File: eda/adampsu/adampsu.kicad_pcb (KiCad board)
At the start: 2 copper layers, 12 parts, among them J1 Barrel_Jack_Switch, U1 LM27761, U2 LT1084-5.0

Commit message: BOM completeled but using expensive LDO
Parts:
- removed C1, C5, C6: 4.7uF, Capacitor_SMD:C_1206_3216Metric_Pad1.42x1.75mm_HandSolder
- removed C2: 1uF, Capacitor_SMD:C_0603_1608Metric_Pad1.05x0.95mm_HandSolder
- removed C3: 10uF, Capacitor_SMD:C_1206_3216Metric_Pad1.42x1.75mm_HandSolder
- removed C4: 22uF, Capacitor_SMD:C_1206_3216Metric_Pad1.42x1.75mm_HandSolder
- removed D1: B240, Diode_SMD:D_SMB
- removed J1: Barrel_Jack_Switch, Connector_BarrelJack:BarrelJack_Horizontal
- removed R1: 1.55M, Capacitor_SMD:C_0603_1608Metric_Pad1.05x0.95mm_HandSolder
- removed R2: 500k, Capacitor_SMD:C_0603_1608Metric_Pad1.05x0.95mm_HandSolder
- removed U1: LM27761, Package_SON:WSON-8-1EP_2x2mm_P0.5mm_EP0.9x1.6mm
- removed U2: LT1084-5.0, Package_TO_SOT_THT:TO-220-3_Vertical

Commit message: Final parts selection finished
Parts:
- added C1: 4.7uF, Capacitor_SMD:C_1206_3216Metric_Pad1.42x1.75mm_HandSolder, F.Cu at (139.4, 106.6)
- added C10: 0.01uF, Capacitor_SMD:C_0603_1608Metric_Pad1.05x0.95mm_HandSolder, F.Cu at (143.3, 109.5)
- added C11: 2200pF, Capacitor_SMD:C_0603_1608Metric_Pad1.05x0.95mm_HandSolder, F.Cu at (144.5, 106.2)
- added C12: 22pF, Capacitor_SMD:C_0603_1608Metric_Pad1.05x0.95mm_HandSolder, F.Cu at (134.7, 113.7)
- added C13: 47uF, Capacitor_SMD:C_1210_3225Metric_Pad1.42x2.65mm_HandSolder, F.Cu at (133.4, 110.3)
- added C14: 47uF, Capacitor_SMD:C_1210_3225Metric_Pad1.42x2.65mm_HandSolder, F.Cu at (157.9, 90.5)
- added C15: 0.01uF, Capacitor_SMD:C_0603_1608Metric_Pad1.05x0.95mm_HandSolder, F.Cu at (153.6, 96.4)
- added C16: 0.1uF, Capacitor_SMD:C_0603_1608Metric_Pad1.05x0.95mm_HandSolder, F.Cu at (163.0, 89.7)
- added C2: 1uF, Capacitor_SMD:C_0603_1608Metric_Pad1.05x0.95mm_HandSolder, F.Cu at (157.9, 93.9)
- added C3: 100uF, Capacitor_THT:CP_Radial_D8.0mm_P3.50mm, F.Cu at (158.1, 83.7)
- added C4: 4.7uF, Capacitor_SMD:C_1206_3216Metric_Pad1.42x1.75mm_HandSolder, F.Cu at (108.8, 112.5)
- added C5: 10uF, Capacitor_SMD:C_0805_2012Metric_Pad1.15x1.40mm_HandSolder, F.Cu at (130.2, 113.9)
- added C6: 4.7uF, Capacitor_SMD:C_1206_3216Metric_Pad1.42x1.75mm_HandSolder, F.Cu at (102.8, 112.5)
- added C7: 4.7uF, Capacitor_SMD:C_1206_3216Metric_Pad1.42x1.75mm_HandSolder, F.Cu at (133.4, 106.6)
- added C8: 0.01uF, Capacitor_SMD:C_0603_1608Metric_Pad1.05x0.95mm_HandSolder, F.Cu at (153.6, 93.9)
- added C9: 0.1uF, adampsu:C_0508_1220Metric_Pad1.40x1.15mm_HandSolder, F.Cu at (138.8, 110.0)
- added D1: D_Schottky, Diode_SMD:D_SMC_Handsoldering, F.Cu at (107.3, 106.9)
- added D2: D_Schottky, Diode_SMD:D_SMC_Handsoldering, F.Cu at (107.3, 97.8)
- added J1: Barrel_Jack_Switch, adampsu:BarrelJack_CUI_PJ-047AH_Horizontal, F.Cu at (145.8, 95.3)
- added J2: Conn_2Rows-09Pins, Connector_PinHeader_2.54mm:PinHeader_2x05_P2.54mm_Vertical, F.Cu at (117.0, 96.3)
- added J3: DB9_Female, Connector_Dsub:DSUB-9_Female_Vertical_P2.77x2.84mm_MountingHoles, F.Cu at (121.9, 85.2)
- added L1: 4.7uH, adampsu:L_11.5x10.3_H4.8, F.Cu at (147.6, 84.9)
- added PC1: PlungerCap, adampsu:PlungerCap-4JWHT, F.Cu at (121.2, 109.5)
- added Q1: BUK7880-55A_CUX, Package_TO_SOT_SMD:SOT-223-3_TabPin2, F.Cu at (126.8, 98.1)
- added R1: 1.55M, Resistor_SMD:R_0603_1608Metric_Pad1.05x0.95mm_HandSolder, F.Cu at (153.6, 103.9)
- added R10: 1.96k, Resistor_SMD:R_0603_1608Metric_Pad1.05x0.95mm_HandSolder, F.Cu at (139.1, 113.1)
- added R2: 500k, Resistor_SMD:R_0603_1608Metric_Pad1.05x0.95mm_HandSolder, F.Cu at (147.7, 108.7)
- added R3: 1k, Resistor_SMD:R_0603_1608Metric_Pad1.05x0.95mm_HandSolder, F.Cu at (143.4, 112.0)
- added R4: 10k, Resistor_SMD:R_0603_1608Metric_Pad1.05x0.95mm_HandSolder, F.Cu at (157.9, 98.9)
- added R5: 665k, Resistor_SMD:R_0603_1608Metric_Pad1.05x0.95mm_HandSolder, F.Cu at (153.6, 98.9)
- added R6: 130k, Resistor_SMD:R_0603_1608Metric_Pad1.05x0.95mm_HandSolder, F.Cu at (163.0, 92.2)
- added R7: 37.4k, Resistor_SMD:R_0603_1608Metric_Pad1.05x0.95mm_HandSolder, F.Cu at (153.6, 101.4)
- added R8: 51.1, Resistor_SMD:R_0603_1608Metric_Pad1.05x0.95mm_HandSolder, F.Cu at (157.9, 96.4)
- added R9: 10.2k, Resistor_SMD:R_0603_1608Metric_Pad1.05x0.95mm_HandSolder, F.Cu at (148.9, 106.2)
- added SW1: 30V 300mA Latching Switch, adampsu:Switch-LC1258EENP, F.Cu at (136.3, 86.1)
- added U1: LM27761, Package_SON:WSON-8-1EP_2x2mm_P0.5mm_EP0.9x1.6mm, F.Cu at (157.9, 101.9)
- added U2: TPS54531DDAR, Package_SO:TI_SO-PowerPAD-8_ThermalVias, F.Cu at (126.2, 105.5)

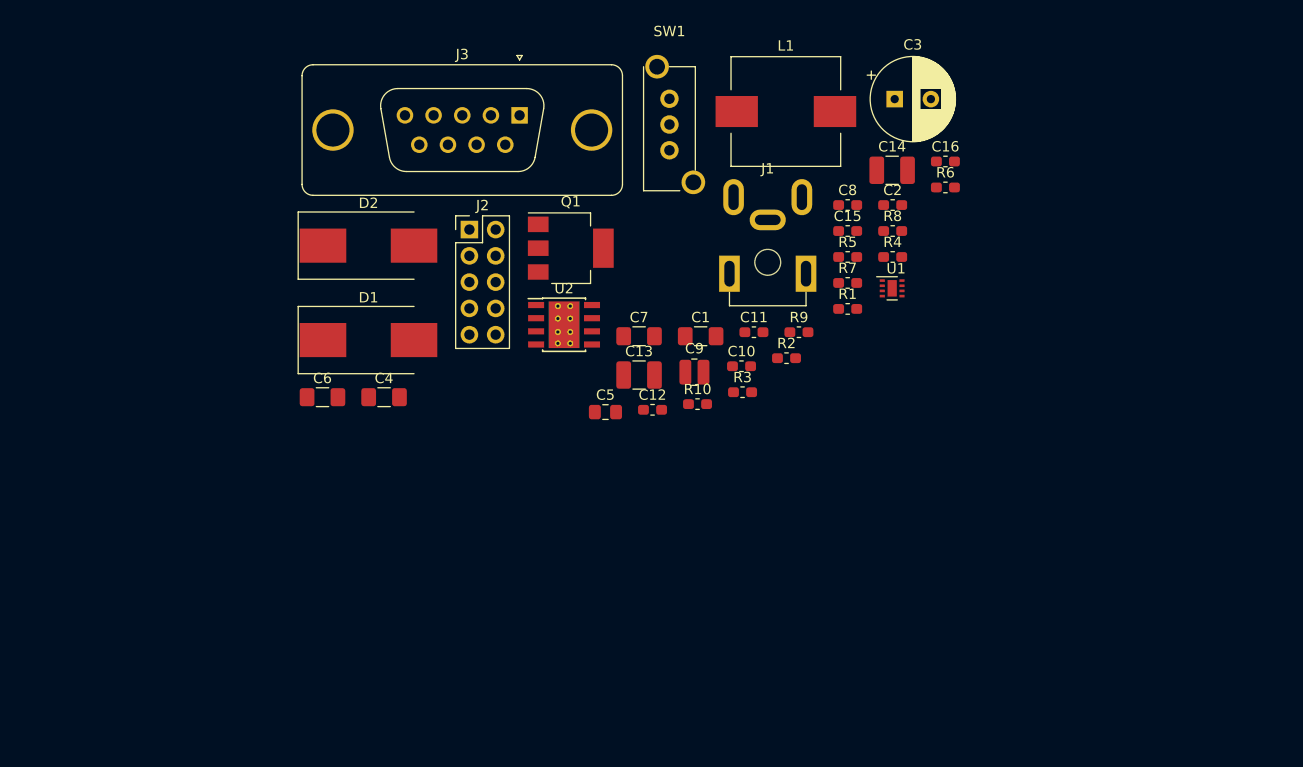
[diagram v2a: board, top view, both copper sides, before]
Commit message: board layout started, but need new -5V regulator
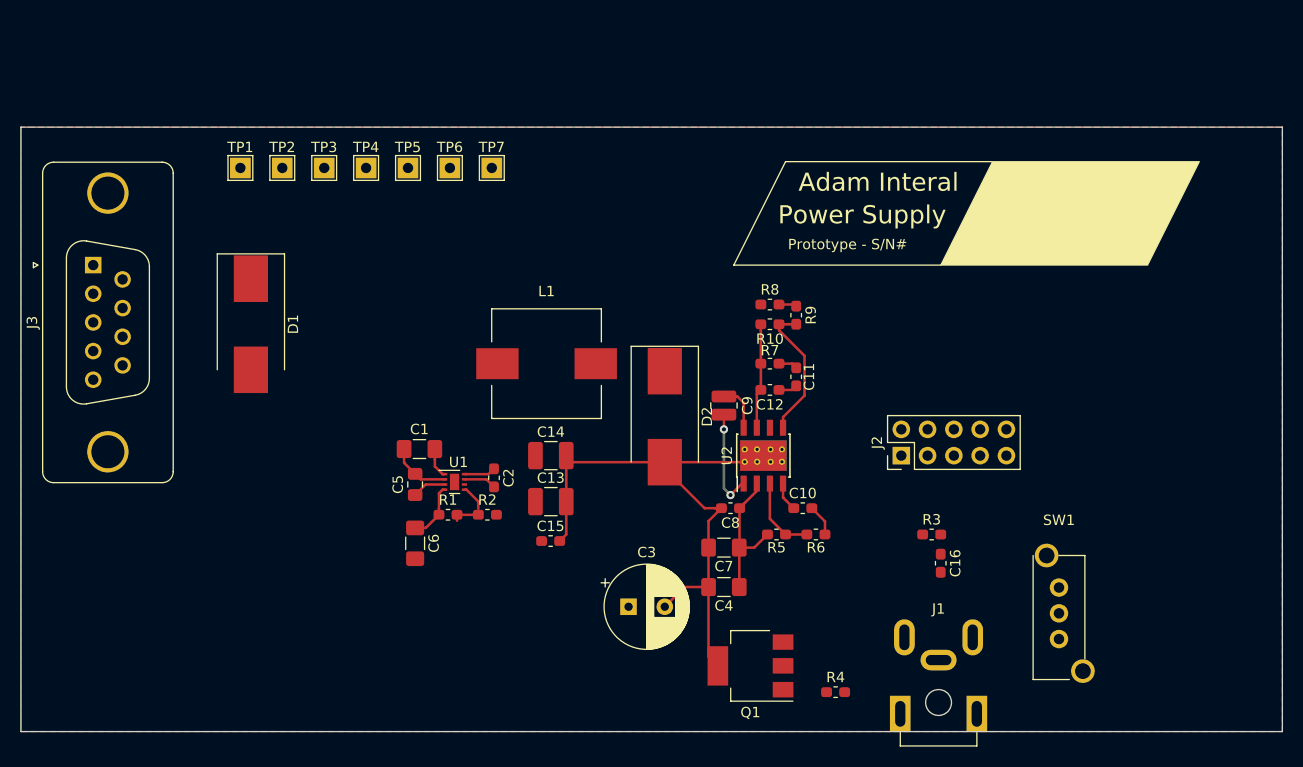
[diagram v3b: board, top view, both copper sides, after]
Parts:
- added LB1: HandLabel_SN, adampsu:adamlabel, F.Cu at (162.6, 99.7)
- added TP1: TestPoint, TestPoint:TestPoint_THTPad_2.0x2.0mm_Drill1.0mm, F.Cu at (94.9, 90.3)
- added TP2: TestPoint, TestPoint:TestPoint_THTPad_2.0x2.0mm_Drill1.0mm, F.Cu at (98.9, 90.3)
- added TP3: TestPoint, TestPoint:TestPoint_THTPad_2.0x2.0mm_Drill1.0mm, F.Cu at (103.0, 90.3)
- added TP4: TestPoint, TestPoint:TestPoint_THTPad_2.0x2.0mm_Drill1.0mm, F.Cu at (107.0, 90.3)
- added TP5: TestPoint, TestPoint:TestPoint_THTPad_2.0x2.0mm_Drill1.0mm, F.Cu at (111.1, 90.3)
- added TP6: TestPoint, TestPoint:TestPoint_THTPad_2.0x2.0mm_Drill1.0mm, F.Cu at (115.1, 90.3)
- added TP7: TestPoint, TestPoint:TestPoint_THTPad_2.0x2.0mm_Drill1.0mm, F.Cu at (119.2, 90.3)
- moved PC1 64.6 mm to (174.0, 146.7)
- moved SW1 60.4 mm to (174.0, 133.3)
- moved C3 55.4 mm to (132.4, 132.7)
- moved J2 47.1 mm to (158.8, 118.1), turned to 90 degrees
- moved C2 46.7 mm to (119.4, 120.3), turned to 270 degrees
- moved U1 46.2 mm to (115.6, 120.7)
- moved J1 45.6 mm to (162.4, 137.9)
- moved Q1 43.9 mm to (144.2, 138.4), turned to 180 degrees
- moved J3 43.7 mm to (80.6, 99.7), turned to 90 degrees
- moved R1 43.5 mm to (114.9, 123.8)
- moved C14 43.0 mm to (124.9, 118.1)
- moved R4 42.4 mm to (152.4, 141.0)
- moved C15 41.5 mm to (124.9, 126.4)
- moved C16 38.8 mm to (162.6, 128.5), turned to 270 degrees
- moved C4 37.6 mm to (141.6, 130.8), turned to 180 degrees
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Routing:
- net GND: track 0.00 -> 76.1 mm
- net +12V: track 0.00 -> 13.9 mm
- net Net-(R10-Pad1): track 0.00 -> 13.5 mm
- net Net-(C9-Pad2): track 0.00 -> 9.77 mm, vias 0 -> 2
- net Net-(R5-Pad2): track 0.00 -> 7.61 mm
- net Net-(C6-Pad1): track 0.00 -> 5.60 mm
- net Net-(R1-Pad2): track 0.00 -> 5.16 mm
- net Net-(C9-Pad1): track 0.00 -> 4.57 mm
- net Net-(C5-Pad1): track 0.00 -> 3.28 mm
- net Net-(C2-Pad2): track 0.00 -> 3.16 mm
- net Net-(C2-Pad1): track 0.00 -> 3.08 mm
- net +5V: track 0.00 -> 2.94 mm
- net Net-(C10-Pad1): track 0.00 -> 2.81 mm
- net Net-(C11-Pad1): track 0.00 -> 1.83 mm
- net Net-(C11-Pad2): track 0.00 -> 1.83 mm
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- added copper zone on F.Cu, net GND
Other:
- board outline added: 121.9 x 58.4 mm

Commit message: Cleanup
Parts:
- added C17: 22uF, Capacitor_SMD:C_1206_3216Metric_Pad1.42x1.75mm_HandSolder, F.Cu at (113.3, 139.8)
- added C18: 22uF, Capacitor_SMD:C_1206_3216Metric_Pad1.42x1.75mm_HandSolder, F.Cu at (121.9, 139.8)
- added C19: 22uF, Capacitor_SMD:C_1206_3216Metric_Pad1.42x1.75mm_HandSolder, F.Cu at (135.6, 113.4)
- added C20: 22uF, Capacitor_SMD:C_1206_3216Metric_Pad1.42x1.75mm_HandSolder, F.Cu at (132.4, 113.4)
- added L2: 4.7uH, adampsu:L_11.5x10.3_H4.8, F.Cu at (117.4, 131.1)
- added R11: 54.9k, Resistor_SMD:R_0603_1608Metric_Pad1.05x0.95mm_HandSolder, F.Cu at (121.9, 114.3)
- added REF**: DB9-SpotMount, adampsu:DB9-SpotMount, F.Cu at (138.0, 159.0)
- added TP10: +5V, adampsu:TestPoint_Labeled, F.Cu at (129.5, 112.0)
- added TP11: GND, adampsu:TestPoint_Labeled, F.Cu at (127.0, 112.0)
- added TP12: GND/Green, adampsu:TestPoint_Labeled, F.Cu at (103.6, 102.9)
- added TP8: GND, adampsu:TestPoint_Labeled, F.Cu at (106.7, 123.2)
- added TP9: -5V, adampsu:TestPoint_Labeled, F.Cu at (109.2, 123.2)
- C1: value 4.7uF -> 10uF; footprint Capacitor_SMD:C_1206_3216Metric_Pad1.42x1.75mm_HandSolder -> Capacitor_SMD:C_0805_2012Metric_Pad1.15x1.40mm_HandSolder
- C13, C14: value 47uF -> 22uF; footprint Capacitor_SMD:C_1210_3225Metric_Pad1.42x2.65mm_HandSolder -> Capacitor_SMD:C_1206_3216Metric_Pad1.42x1.75mm_HandSolder
- C2: value 1uF -> 10uF; footprint Capacitor_SMD:C_0603_1608Metric_Pad1.05x0.95mm_HandSolder -> Capacitor_SMD:C_0805_2012Metric_Pad1.15x1.40mm_HandSolder
- C3: footprint Capacitor_THT:CP_Radial_D8.0mm_P3.50mm -> Capacitor_Tantalum_SMD:CP_EIA-7343-43_Kemet-X_Pad2.25x2.55mm_HandSolder
- C4, C7: footprint Capacitor_SMD:C_1206_3216Metric_Pad1.42x1.75mm_HandSolder -> Capacitor_SMD:C_0805_2012Metric_Pad1.15x1.40mm_HandSolder
- C5: value 10uF -> 0.1uF; footprint Capacitor_SMD:C_0805_2012Metric_Pad1.15x1.40mm_HandSolder -> Capacitor_SMD:C_0603_1608Metric_Pad1.05x0.95mm_HandSolder
- C6: value 4.7uF -> 0.1uF; footprint Capacitor_SMD:C_1206_3216Metric_Pad1.42x1.75mm_HandSolder -> adampsu:C_0508_1220Metric_Pad1.40x1.15mm_HandSolder
- D1, D2: footprint Diode_SMD:D_SMC_Handsoldering -> adampsu:D_SOD-128
- LB1: moved to B.Cu
- R1: value 1.55M -> 10k
- R2: value 500k -> 10k
- TP1: value TestPoint -> +12VL/Orange; footprint TestPoint:TestPoint_THTPad_2.0x2.0mm_Drill1.0mm -> adampsu:TestPoint_Labeled
- TP2: value TestPoint -> RESET/Black; footprint TestPoint:TestPoint_THTPad_2.0x2.0mm_Drill1.0mm -> adampsu:TestPoint_Labeled
- TP3: value TestPoint -> +12VI/Yellow; footprint TestPoint:TestPoint_THTPad_2.0x2.0mm_Drill1.0mm -> adampsu:TestPoint_Labeled
- TP4: value TestPoint -> DATA/Brown; footprint TestPoint:TestPoint_THTPad_2.0x2.0mm_Drill1.0mm -> adampsu:TestPoint_Labeled
- TP5: value TestPoint -> +5V/Red; footprint TestPoint:TestPoint_THTPad_2.0x2.0mm_Drill1.0mm -> adampsu:TestPoint_Labeled
- TP6: value TestPoint -> GND/Green; footprint TestPoint:TestPoint_THTPad_2.0x2.0mm_Drill1.0mm -> adampsu:TestPoint_Labeled
- TP7: value TestPoint -> -5V/Blue; footprint TestPoint:TestPoint_THTPad_2.0x2.0mm_Drill1.0mm -> adampsu:TestPoint_Labeled
- U1: value LM27761 -> TPS561201; footprint Package_SON:WSON-8-1EP_2x2mm_P0.5mm_EP0.9x1.6mm -> Package_TO_SOT_SMD:SOT-23-6_Handsoldering
- moved J2 59.5 mm to (103.0, 139.0), turned to 0 degrees
- moved PC1 36.2 mm to (143.5, 166.3)
- moved R3 36.1 mm to (130.2, 143.3), turned to 90 degrees
- moved SW1 34.8 mm to (141.8, 146.5)
- moved J1 33.3 mm to (131.8, 151.1)
- moved C16 32.6 mm to (133.0, 142.2), turned to 0 degrees
- moved J3 29.4 mm to (96.5, 124.5), turned to 270 degrees
- moved TP2 27.3 mm to (123.2, 102.9)
- moved L1 22.3 mm to (145.1, 117.7)
- moved TP1 21.3 mm to (112.0, 102.9)
- moved C7 19.9 mm to (158.8, 137.0), turned to 0 degrees
- moved R4 19.7 mm to (133.0, 144.1)
- moved C3 19.6 mm to (151.3, 138.0), turned to 180 degrees
- moved LB1 19.3 mm to (165.7, 118.7), turned to 270 degrees
- moved C4 19.2 mm to (158.8, 139.5), turned to 0 degrees
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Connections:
- net Net-(C9-Pad1) renamed /PH
- C1 pad 1: +5V -> +12V
- C14 pad 1: +5V -> GND
- C14 pad 2: GND -> +5V
- C2 pad 1: Net-(C2-Pad1) -> +12V
- C2 pad 2: Net-(C2-Pad2) -> GND
- C5 pad 1: Net-(C5-Pad1) -> +12V
- C6 pad 2: GND -> /SW
- D1 pad 1: /+12VI -> +12V
- J3 pad 1: /+12VL -> +12V
- J3 pad 2: /+12VI -> +12V
- R1 pad 1: Net-(C6-Pad1) -> GND
- R2 pad 1: Net-(R1-Pad2) -> /-5V
- R2 pad 2: GND -> Net-(R11-Pad2)
- TP1 pad 1: /+12VL -> +12V
- TP3 pad 1: /+12VI -> +12V
- U1 pad 1: +5V -> /-5V
- U1 pad 2: GND -> /SW
- U1 pad 3: Net-(C5-Pad1) -> +12V
- U1 pad 4: Net-(C6-Pad1) -> Net-(R11-Pad2)
- U1 pad 6: Net-(U1-Pad6) -> Net-(C6-Pad1)
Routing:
- net GND: track 76.1 -> 253.2 mm, vias 0 -> 16
- net +12V: track 13.9 -> 164.4 mm, vias 0 -> 4
- net +5V: track 2.94 -> 96.8 mm, vias 0 -> 5
- net /RESET: track 0.00 -> 86.0 mm
- net /DATA: track 0.00 -> 78.1 mm, vias 0 -> 1
- net /-5V: track 0.00 -> 77.2 mm
- net Net-(C16-Pad1): track 0.00 -> 16.4 mm, vias 0 -> 1
- net /GND-F: track 0.00 -> 13.2 mm
- net /SW: track 0.00 -> 11.5 mm
- net /PH: track 4.57 -> 15.4 mm
- net Net-(R11-Pad2): track 0.00 -> 10.2 mm, vias 0 -> 2
- net Net-(Q1-Pad1): track 0.00 -> 7.58 mm
- net Net-(C11-Pad1): track 1.83 -> 7.88 mm
- net Net-(C5-Pad1): track 3.28 -> 0.00 mm
- net Net-(C2-Pad2): track 3.16 -> 0.00 mm
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- added copper zone on F.Cu, net +12V
- added copper zone on B.Cu, net +5V
- added copper zone on F.Cu, net +5V
- added copper zone on F.Cu, net /-5V
- added copper zone on F.Cu, net /PH
- added copper zone on F.Cu, net /SW
- added copper zone on B.Cu, net GND
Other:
- board size 121.9 x 58.4 mm -> 78.7 x 60.8 mm
- net class Default: clearance 0.2 -> 0.2286; trace_width 0.25 -> 0.3048
- net class Power added: clearance 0.2286, trace_width 0.4572, via_dia 0.9144, via_drill 0.6096
- rule trace_clearance: 0.2 -> 0.2286
- board text added: "2019 v0.1"
- board text added: "By Shelby Jueden"
- board text added: "Output Ratings: 12V - Unregulated +5V - 5A -5V - 1A"
- board text added: "https://github.com/AkBKukU/adam-psu"

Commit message: Export schematic and PCB to PDFs
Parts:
- moved C17 47.9 mm to (138.7, 99.2)
- moved C18 47.9 mm to (147.3, 99.2)
- moved SW1 47.9 mm to (167.2, 105.9)
- moved C1 47.9 mm to (146.7, 78.5)
- moved C10 47.9 mm to (188.3, 92.1)
- moved C11 47.9 mm to (185.5, 81.5)
- moved C12 47.9 mm to (185.5, 79.5)
- moved C13 47.9 mm to (161.0, 81.5)
- moved C15 47.9 mm to (154.3, 77.0)
- moved C19 47.9 mm to (161.0, 72.8)
- moved C2 47.9 mm to (149.1, 78.5)
- moved C4 47.9 mm to (184.2, 98.9)
- moved C6 47.9 mm to (140.3, 77.1)
- moved C7 47.9 mm to (184.2, 96.4)
- moved C8 47.9 mm to (179.5, 93.9)
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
